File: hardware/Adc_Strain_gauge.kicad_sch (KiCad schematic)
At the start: 16 parts, among them J12 Load Cell 2, J4 Load Cell 3, J6 Load Cell 1, U3 ADS131M03IRUKx

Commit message: Fixed ERC errors & CAN module
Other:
- note added: "STRAIN GAUGES AND ADC"
- moved on the sheet: C11, C12, C13, C14, C8, C9, J12, J4, J6, R12, R13, R14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

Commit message: Added EEPROM, resolved comments
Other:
- note removed: "STRAIN GAUGES AND ADC"
- company: (none) -> University of Toronto Human Powered Vehicles
- title: (none) -> Strain gauges & ADC
- moved on the sheet: C11, C12, C13, C14, C8, C9, J12, J4, J6, R12, R13, R14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

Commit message: Stylistic changes
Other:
- moved on the sheet: C11, C12, C8, J12, J4, J6, R12, R13, R16, R17

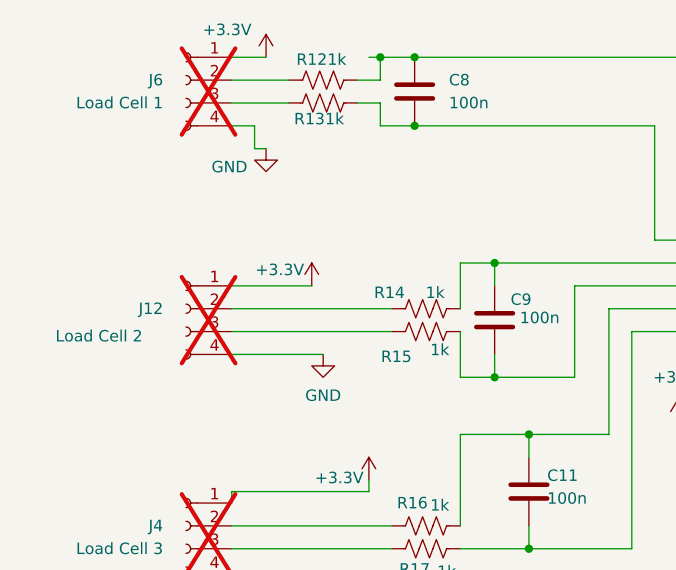
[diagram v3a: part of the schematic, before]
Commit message: modified mcu pin alloc and pre-routing placement
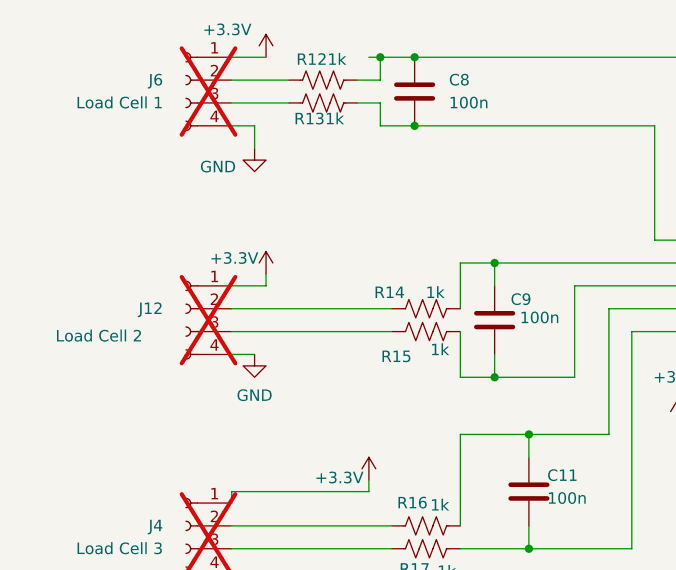
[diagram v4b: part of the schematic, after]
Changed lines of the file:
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@@
-	(wire
-		(pts
-			(xy 52.07 59.69) (xy 60.96 59.69)
-		)
-		(stroke
-			(width 0)
-			(type default)
-		)
-	)
 	(wire
 		(pts
@@
 	(wire
 		(pts
-			(xy 54.61 44.45) (xy 55.88 44.45)
-		)
-		(stroke
-			(width 0)
-			(type default)
-		)
-	)
-	(wire
-		(pts
 			(xy 77.47 76.2) (xy 77.47 86.36)
 		)
@@
 	(wire
 		(pts
+			(xy 55.88 58.42) (xy 55.88 59.69)
+		)
+		(stroke
+			(width 0)
+			(type default)
+		)
+	)
+	(wire
+		(pts
+			(xy 55.88 59.69) (xy 52.07 59.69)
+		)
+		(stroke
+			(width 0)
+			(type default)
+		)
+	)
+	(wire
+		(pts
 			(xy 77.47 69.85) (xy 81.28 69.85)
 		)
@@
 	(wire
 		(pts
-			(xy 52.07 67.31) (xy 62.23 67.31)
+			(xy 52.07 67.31) (xy 54.61 67.31)
 		)
 		(stroke
@@
 	(symbol
 		(lib_id "power:GND")
-		(at 62.23 67.31 0)
+		(at 54.61 67.31 0)
 		(unit 1)
 		(exclude_from_sim no)
@@
 		(dnp no)
 		(property "Reference" "#PWR044"
-			(at 62.23 73.66 0)
+			(at 54.61 73.66 0)
 			(effects
 				(font
@@
 		)
 		(property "Value" "GND"
-			(at 62.23 71.882 0)
+			(at 54.61 71.882 0)
 			(effects
 				(font
@@
 		)
 		(property "Footprint" ""
-			(at 62.23 67.31 0)
+			(at 54.61 67.31 0)
 			(effects
 				(font
@@
 		)
 		(property "Datasheet" ""
-			(at 62.23 67.31 0)
+			(at 54.61 67.31 0)
 			(effects
 				(font
@@
 		)
 		(property "Description" "Power symbol creates a global label with name \"GND\" , ground"
-			(at 62.23 67.31 0)
+			(at 54.61 67.31 0)
 			(effects
 				(font
@@
 	(symbol
 		(lib_id "power:GND")
-		(at 55.88 44.45 0)
+		(at 54.61 44.45 0)
 		(unit 1)
 		(exclude_from_sim no)
@@
 		(dnp no)
 		(property "Reference" "#PWR041"
-			(at 55.88 50.8 0)
+			(at 54.61 50.8 0)
 			(effects
 				(font
@@
 		)
 		(property "Value" "GND"
-			(at 51.816 46.482 0)
+			(at 50.546 46.482 0)
 			(effects
 				(font
@@
 		)
 		(property "Footprint" ""
-			(at 55.88 44.45 0)
+			(at 54.61 44.45 0)
 			(effects
 				(font
@@
 		)
 		(property "Datasheet" ""
-			(at 55.88 44.45 0)
+			(at 54.61 44.45 0)
 			(effects
 				(font
@@
 		)
 		(property "Description" "Power symbol creates a global label with name \"GND\" , ground"
-			(at 55.88 44.45 0)
+			(at 54.61 44.45 0)
 			(effects
 				(font
@@
 	(symbol
 		(lib_id "power:+3.3V")
-		(at 60.96 59.69 0)
+		(at 55.88 58.42 0)
 		(unit 1)
 		(exclude_from_sim no)
@@
 		(dnp no)
 		(property "Reference" "#PWR042"
-			(at 60.96 63.5 0)
+			(at 55.88 62.23 0)
 			(effects
 				(font
@@
 		)
 		(property "Value" "+3.3V"
-			(at 57.404 57.912 0)
+			(at 52.324 56.642 0)
 			(effects
 				(font
@@
 		)
 		(property "Footprint" ""
-			(at 60.96 59.69 0)
+			(at 55.88 58.42 0)
 			(effects
 				(font
@@
 		)
 		(property "Datasheet" ""
-			(at 60.96 59.69 0)
+			(at 55.88 58.42 0)
 			(effects
 				(font
@@
 		)
 		(property "Description" "Power symbol creates a global label with name \"+3.3V\""
-			(at 60.96 59.69 0)
-			(effects
-				(font
+			(at 55.88 58.42 0)
+			(effects
+				(font

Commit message: Completed first layout draft
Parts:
- added NT1: NetTie_2, NetTie:NetTie-2_THT_Pad1.0mm, symbol Device:NetTie_2
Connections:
- net AGND: now also NT1.1; no longer C13.2, C14.2, U3.17 (DGND)
- new net GND: C13.2, C14.2, NT1.2, U3.17 (DGND)

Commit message: resolved comments
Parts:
- removed NT1: NetTie_2, NetTie:NetTie-2_THT_Pad1.0mm, symbol Device:NetTie_2
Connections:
- net +3.3V: no longer C12.1, J12.1 (Pin_1), J4.1 (Pin_1), J6.1 (Pin_1), U3.19 (AVDD)
- new net +3.3VA: C12.1, J12.1 (Pin_1), J4.1 (Pin_1), J6.1 (Pin_1), U3.19 (AVDD)
